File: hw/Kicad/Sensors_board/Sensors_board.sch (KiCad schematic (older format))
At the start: 17 parts, among them J1 SENSORES_LINEA, U1 CNY70, U2 CNY70, U3 CNY70, U4 CNY70, U5 CNY70, U6 CNY70, U7 4053

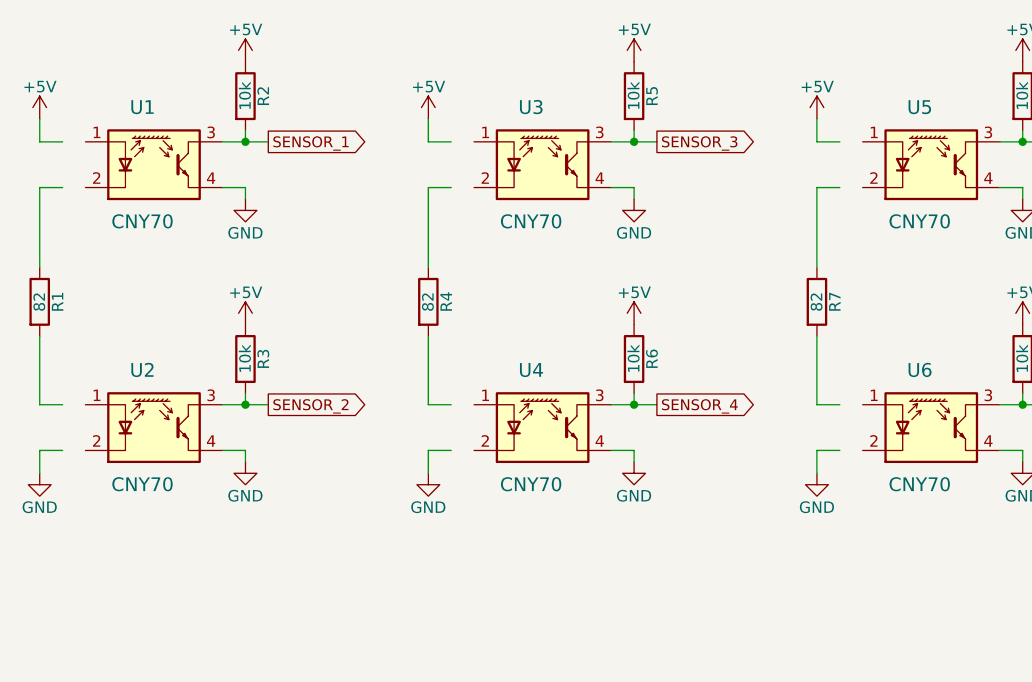
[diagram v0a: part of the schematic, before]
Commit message: PCBs adapted with Kicad libraries models
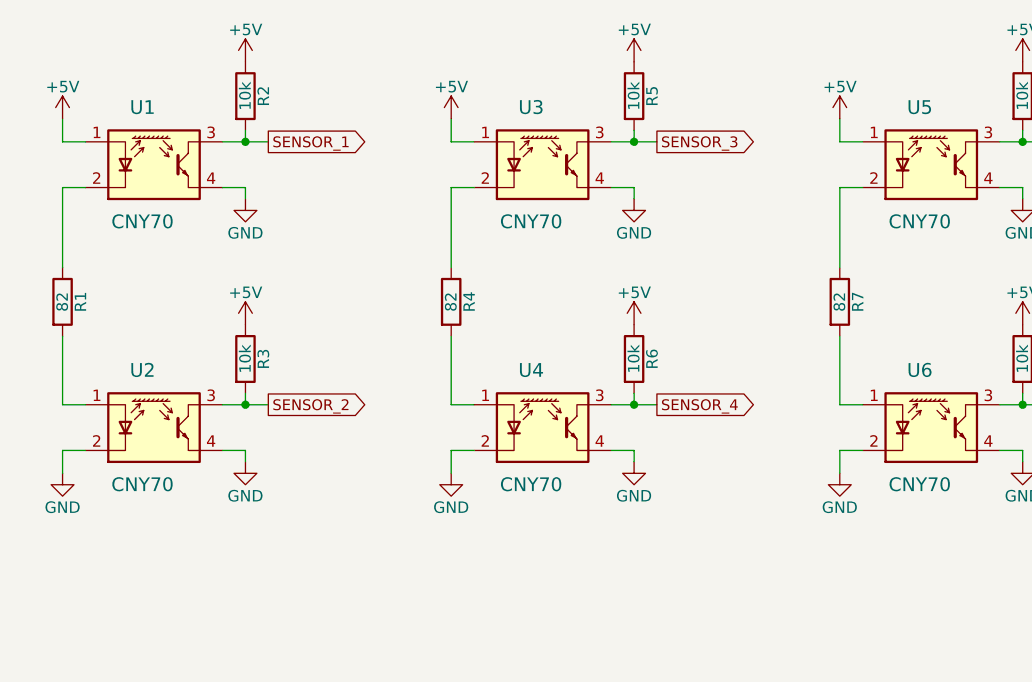
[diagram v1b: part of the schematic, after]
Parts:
- J1: footprint Pin_Headers:Pin_Header_Angled_1x07_Pitch2.54mm -> Sensors_board:PinHeader_1x07_P2.54mm_Horizontal
- R1, R2, R3, R4, R5, R6, R7, R8, R9: footprint Resistors_THT:R_Axial_DIN0207_L6.3mm_D2.5mm_P10.16mm_Horizontal -> Sensors_board:R_Axial_DIN0207_L6.3mm_D2.5mm_P10.16mm_Horizontal
- U1, U2, U3, U4, U5, U6: footprint Sensors_board:CNY70 -> Sensors_board:Vishay_CNY70
- U7: footprint Housings_DIP:DIP-16_W7.62mm_LongPads -> Sensors_board:DIP-16_W7.62mm_Socket_LongPads
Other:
- moved on the sheet: R1, R4, R7
